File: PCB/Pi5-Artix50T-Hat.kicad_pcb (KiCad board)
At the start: 4 copper layers, 85 x 56 mm, 162 parts, among them J1 GPIO, J2 Molex 0878321420, J3 68711614522, J5 MIPI0, J6 MIPI1, U1 BL24C256A, U10 AP62200TWU-7, U11 AP62200TWU-7, U12 AP62200TWU-7, U2 XC7A50T-FGG484, U9 AP62200TWU-7, X1 50MHz

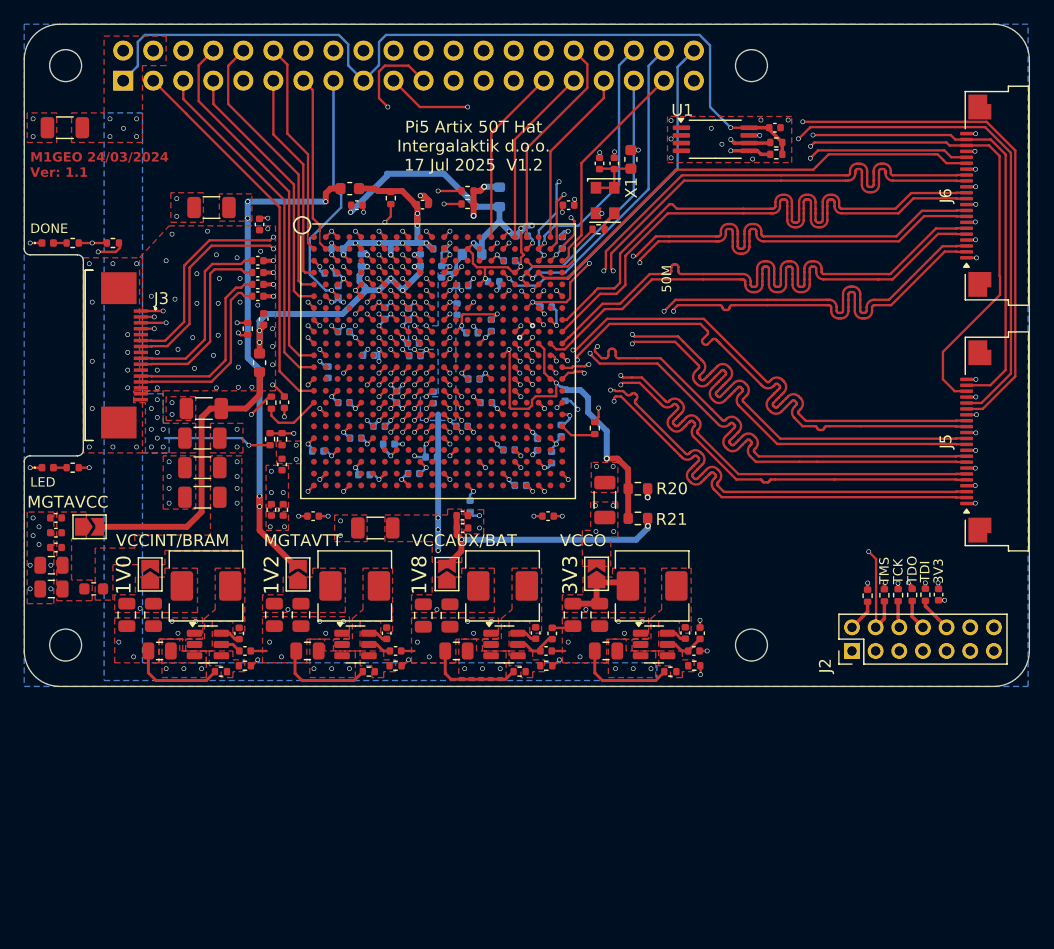
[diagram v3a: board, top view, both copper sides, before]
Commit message: MIPI conectors should be now compatible with C597981
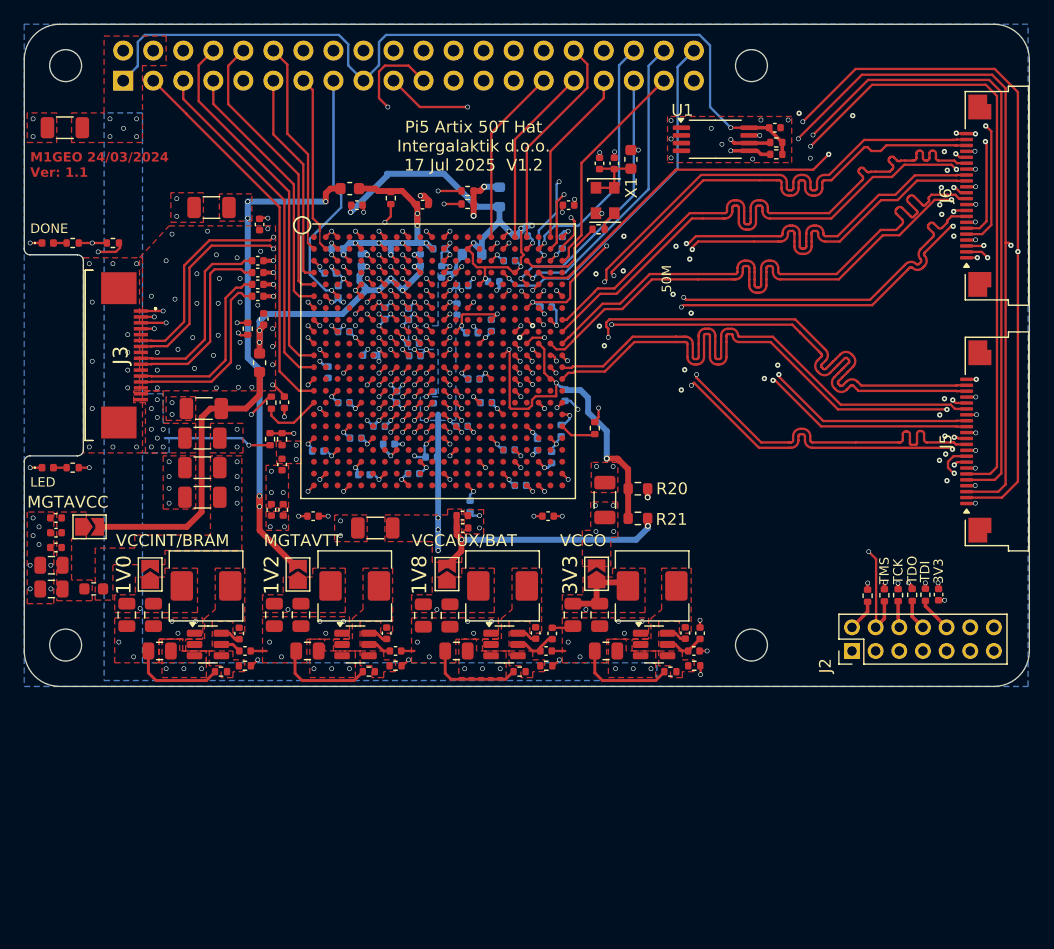
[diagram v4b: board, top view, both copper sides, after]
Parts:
- J3: footprint 68711614522:68711614522 -> Wurth_68711614522:68711614522
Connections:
- J5 pad 1: GND -> BANK_15_VCC
- J5 pad 11: /FPGA Top/FPGA Bank 15 & 16/MIPI0_D2+ -> /FPGA Top/FPGA Bank 15 & 16/MIPI0_D2-
- J5 pad 12: /FPGA Top/FPGA Bank 15 & 16/MIPI0_D2- -> /FPGA Top/FPGA Bank 15 & 16/MIPI0_D2+
- J5 pad 14: /FPGA Top/FPGA Bank 15 & 16/MIPI0_D1+ -> /FPGA Top/FPGA Bank 15 & 16/MIPI0_CK-
- J5 pad 15: /FPGA Top/FPGA Bank 15 & 16/MIPI0_D1- -> /FPGA Top/FPGA Bank 15 & 16/MIPI0_CK+
- J5 pad 17: /FPGA Top/FPGA Bank 15 & 16/MIPI0_CAM_GPIO0 -> /FPGA Top/FPGA Bank 15 & 16/MIPI0_D3-
- J5 pad 18: /FPGA Top/FPGA Bank 15 & 16/MIPI0_CAM_GPIO1 -> /FPGA Top/FPGA Bank 15 & 16/MIPI0_D3+
- J5 pad 2: /FPGA Top/FPGA Bank 15 & 16/MIPI0_D0+ -> /FPGA Top/FPGA Bank 15 & 16/SDA0
- J5 pad 20: /FPGA Top/FPGA Bank 15 & 16/SCL0 -> /FPGA Top/FPGA Bank 15 & 16/MIPI0_D0-
- J5 pad 21: /FPGA Top/FPGA Bank 15 & 16/SDA0 -> /FPGA Top/FPGA Bank 15 & 16/MIPI0_D0+
- J5 pad 22: BANK_15_VCC -> GND
- J5 pad 3: /FPGA Top/FPGA Bank 15 & 16/MIPI0_D0- -> /FPGA Top/FPGA Bank 15 & 16/SCL0
- J5 pad 5: /FPGA Top/FPGA Bank 15 & 16/MIPI0_D3+ -> /FPGA Top/FPGA Bank 15 & 16/MIPI0_CAM_GPIO1
- J5 pad 6: /FPGA Top/FPGA Bank 15 & 16/MIPI0_D3- -> /FPGA Top/FPGA Bank 15 & 16/MIPI0_CAM_GPIO0
- J5 pad 8: /FPGA Top/FPGA Bank 15 & 16/MIPI0_CK+ -> /FPGA Top/FPGA Bank 15 & 16/MIPI0_D1-
- J5 pad 9: /FPGA Top/FPGA Bank 15 & 16/MIPI0_CK- -> /FPGA Top/FPGA Bank 15 & 16/MIPI0_D1+
- J6 pad 1: GND -> BANK_15_VCC
- J6 pad 11: /FPGA Top/FPGA Bank 15 & 16/MIPI1_D2+ -> /FPGA Top/FPGA Bank 15 & 16/MIPI1_D2-
- J6 pad 12: /FPGA Top/FPGA Bank 15 & 16/MIPI1_D2- -> /FPGA Top/FPGA Bank 15 & 16/MIPI1_D2+
- J6 pad 14: /FPGA Top/FPGA Bank 15 & 16/MIPI1_D1+ -> /FPGA Top/FPGA Bank 15 & 16/MIPI1_CK-
- J6 pad 15: /FPGA Top/FPGA Bank 15 & 16/MIPI1_D1- -> /FPGA Top/FPGA Bank 15 & 16/MIPI1_CK+
- J6 pad 17: /FPGA Top/FPGA Bank 15 & 16/MIPI1_CAM_GPIO0 -> /FPGA Top/FPGA Bank 15 & 16/MIPI1_D3-
- J6 pad 18: /FPGA Top/FPGA Bank 15 & 16/MIPI1_CAM_GPIO1 -> /FPGA Top/FPGA Bank 15 & 16/MIPI1_D3+
- J6 pad 2: /FPGA Top/FPGA Bank 15 & 16/MIPI1_D0+ -> /FPGA Top/FPGA Bank 15 & 16/SDA0
- J6 pad 20: /FPGA Top/FPGA Bank 15 & 16/SCL0 -> /FPGA Top/FPGA Bank 15 & 16/MIPI1_D0-
- J6 pad 21: /FPGA Top/FPGA Bank 15 & 16/SDA0 -> /FPGA Top/FPGA Bank 15 & 16/MIPI1_D0+
- J6 pad 22: BANK_15_VCC -> GND
- J6 pad 3: /FPGA Top/FPGA Bank 15 & 16/MIPI1_D0- -> /FPGA Top/FPGA Bank 15 & 16/SCL0
- J6 pad 5: /FPGA Top/FPGA Bank 15 & 16/MIPI1_D3+ -> /FPGA Top/FPGA Bank 15 & 16/MIPI1_CAM_GPIO1
- J6 pad 6: /FPGA Top/FPGA Bank 15 & 16/MIPI1_D3- -> /FPGA Top/FPGA Bank 15 & 16/MIPI1_CAM_GPIO0
- J6 pad 8: /FPGA Top/FPGA Bank 15 & 16/MIPI1_CK+ -> /FPGA Top/FPGA Bank 15 & 16/MIPI1_D1-
- J6 pad 9: /FPGA Top/FPGA Bank 15 & 16/MIPI1_CK- -> /FPGA Top/FPGA Bank 15 & 16/MIPI1_D1+
- U2 pad B21: /FPGA Top/FPGA Bank 15 & 16/SCL0 -> /FPGA Top/FPGA Bank 15 & 16/MIPI0_CAM_GPIO0
- U2 pad C20: /FPGA Top/FPGA Bank 15 & 16/SDA0 -> /FPGA Top/FPGA Bank 15 & 16/MIPI0_CAM_GPIO1
- U2 pad F19: /FPGA Top/FPGA Bank 15 & 16/MIPI0_CAM_GPIO0 -> /FPGA Top/FPGA Bank 15 & 16/SDA0
- U2 pad F20: /FPGA Top/FPGA Bank 15 & 16/MIPI0_CAM_GPIO1 -> /FPGA Top/FPGA Bank 15 & 16/SCL0
- U2 pad G20: /FPGA Top/FPGA Bank 15 & 16/MIPI1_D1- -> /FPGA Top/FPGA Bank 15 & 16/MIPI1_D0-
- U2 pad H20: /FPGA Top/FPGA Bank 15 & 16/MIPI1_D1+ -> /FPGA Top/FPGA Bank 15 & 16/MIPI1_D0+
- U2 pad H22: /FPGA Top/FPGA Bank 15 & 16/MIPI1_D2- -> /FPGA Top/FPGA Bank 15 & 16/MIPI1_D3-
- U2 pad J22: /FPGA Top/FPGA Bank 15 & 16/MIPI1_D2+ -> /FPGA Top/FPGA Bank 15 & 16/MIPI1_D3+
- U2 pad K21: /FPGA Top/FPGA Bank 15 & 16/MIPI1_D3+ -> /FPGA Top/FPGA Bank 15 & 16/MIPI1_D2+
- U2 pad K22: /FPGA Top/FPGA Bank 15 & 16/MIPI1_D3- -> /FPGA Top/FPGA Bank 15 & 16/MIPI1_D2-
- U2 pad L18: /FPGA Top/FPGA Bank 15 & 16/MIPI0_D3- -> /FPGA Top/FPGA Bank 15 & 16/MIPI0_D2-
- U2 pad L19: /FPGA Top/FPGA Bank 15 & 16/MIPI0_D1+ -> /FPGA Top/FPGA Bank 15 & 16/MIPI0_D0+
- U2 pad L20: /FPGA Top/FPGA Bank 15 & 16/MIPI0_D1- -> /FPGA Top/FPGA Bank 15 & 16/MIPI0_D0-
- U2 pad L21: /FPGA Top/FPGA Bank 15 & 16/MIPI1_D0- -> /FPGA Top/FPGA Bank 15 & 16/MIPI1_D1-
- U2 pad M18: /FPGA Top/FPGA Bank 15 & 16/MIPI0_D3+ -> /FPGA Top/FPGA Bank 15 & 16/MIPI0_D2+
- U2 pad M21: /FPGA Top/FPGA Bank 15 & 16/MIPI1_D0+ -> /FPGA Top/FPGA Bank 15 & 16/MIPI1_D1+
- U2 pad M22: /FPGA Top/FPGA Bank 15 & 16/MIPI0_D2- -> /FPGA Top/FPGA Bank 15 & 16/MIPI0_D3-
- U2 pad N18: /FPGA Top/FPGA Bank 15 & 16/MIPI0_D0+ -> /FPGA Top/FPGA Bank 15 & 16/MIPI0_D1+
- U2 pad N19: /FPGA Top/FPGA Bank 15 & 16/MIPI0_D0- -> /FPGA Top/FPGA Bank 15 & 16/MIPI0_D1-
- U2 pad N22: /FPGA Top/FPGA Bank 15 & 16/MIPI0_D2+ -> /FPGA Top/FPGA Bank 15 & 16/MIPI0_D3+
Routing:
- net /FPGA Top/FPGA Bank 15 & 16/SDA0: track 69.9 -> 99.2 mm, vias 3 -> 4
- net /FPGA Top/FPGA Bank 15 & 16/SCL0: track 67.5 -> 95.6 mm, vias 2 -> 4
- net /FPGA Top/FPGA Bank 15 & 16/MIPI1_CAM_GPIO1: track 39.2 -> 52.5 mm, vias 2 -> 3
- net /FPGA Top/FPGA Bank 15 & 16/MIPI1_CAM_GPIO0: track 41.0 -> 51.5 mm, vias 0 -> 2
- net /FPGA Top/FPGA Bank 15 & 16/MIPI0_CAM_GPIO1: track 76.7 -> 84.6 mm, vias 2 -> 3
- net /FPGA Top/FPGA Bank 15 & 16/MIPI1_D3+: track 49.8 -> 46.9 mm, vias 0 -> 2
- net /FPGA Top/FPGA Bank 15 & 16/MIPI1_D2+: track 49.8 -> 47.1 mm, vias 0 -> 2
- net /FPGA Top/FPGA Bank 15 & 16/MIPI0_D2+: track 47.2 -> 44.5 mm, vias 2 -> 4
- net /FPGA Top/FPGA Bank 15 & 16/MIPI1_D1+: track 47.0 -> 44.3 mm, vias 2 -> 4
- net /FPGA Top/FPGA Bank 15 & 16/MIPI0_D1+: track 49.5 -> 47.1 mm
- net /FPGA Top/FPGA Bank 15 & 16/MIPI0_D0+: track 47.2 -> 48.5 mm
- net BANK_15_VCC: track 118.8 -> 120.0 mm
- net /FPGA Top/FPGA Bank 15 & 16/MIPI0_CAM_GPIO0: track 79.1 -> 80.1 mm
- net /FPGA Top/FPGA Bank 15 & 16/MIPI0_D3-: track 47.1 -> 46.4 mm, vias 2 -> 0
- net /FPGA Top/FPGA Bank 15 & 16/MIPI0_D2-: track 46.9 -> 47.5 mm
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
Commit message: Update
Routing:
- net /FPGA Top/FPGA Bank 15 & 16/MIPI0_CK-: track 47.0 -> 47.9 mm
- net /FPGA Top/FPGA Bank 15 & 16/MIPI0_CK+: track 47.1 -> 47.9 mm
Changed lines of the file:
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@@
 		(grid_origin 100 100)
 		(pcbplotparams
-			(layerselection 0x00000000_00000000_55555555_5755f5ff)
-			(plot_on_all_layers_selection 0x00000000_00000000_00000000_00000000)
+			(layerselection 0x00000000_00000000_55555555_575ff5ff)
+			(plot_on_all_layers_selection 0x00000000_00000000_00000000_02000000)
 			(disableapertmacros no)
 			(usegerberextensions yes)
@@
 			(drillshape 0)
 			(scaleselection 1)
-			(outputdirectory "outputs/")
+			(outputdirectory "production/gerbers/")
 		)
 	)
@@
 	)
 	(segment
+		(start 148.497812 68.590386)
+		(end 150.753198 66.335)
+		(width 0.2)
+		(layer "In2.Cu")
+		(net 313)
+	)
+	(segment
 		(start 145.869075 70.67)
 		(end 146.418198 70.67)
@@
 	)
 	(segment
-		(start 155.716801 66.335)
+		(start 157.87 68.488199)
 		(end 157.986946 68.605145)
 		(width 0.2)
@@
 	)
 	(segment
-		(start 148.497812 68.590386)
-		(end 150.753198 66.335)
-		(width 0.2)
-		(layer "In2.Cu")
-		(net 313)
-	)
-	(segment
 		(start 144.16 70.67)
 		(end 144.669075 70.67)
@@
 	)
 	(segment
+		(start 150.753198 66.335)
+		(end 157.125 66.335)
+		(width 0.2)
+		(layer "In2.Cu")
+		(net 313)
+	)
+	(segment
 		(start 163.322512 74.117488)
 		(end 163.322512 73.940711)
@@
 	)
 	(segment
-		(start 146.418198 70.67)
-		(end 146.877817 70.21038)
+		(start 157.125 66.335)
+		(end 157.87 67.08)
 		(width 0.2)
 		(layer "In2.Cu")
@@
 	)
 	(segment
-		(start 150.753198 66.335)
-		(end 155.716801 66.335)
+		(start 157.87 67.08)
+		(end 157.87 68.488199)
+		(width 0.2)
+		(layer "In2.Cu")
+		(net 313)
+	)
+	(segment
+		(start 146.418198 70.67)
+		(end 146.877817 70.21038)
 		(width 0.2)
 		(layer "In2.Cu")
@@
 	)
 	(segment
-		(start 158.305145 68.286946)
-		(end 155.903199 65.885)
+		(start 163.640711 73.622512)
+		(end 162.234014 72.215815)
 		(width 0.2)
 		(layer "In2.Cu")
@@
 	)
 	(segment
-		(start 163.640711 73.622512)
-		(end 162.234014 72.215815)
+		(start 146.381802 70.07)
+		(end 143.33 70.07)
+		(width 0.2)
+		(layer "In2.Cu")
+		(net 314)
+	)
+	(segment
+		(start 158.3 68.281801)
+		(end 158.3 66.91)
 		(width 0.2)
 		(layer "In2.Cu")
@@
 	)
 	(segment
-		(start 150.566802 65.885)
-		(end 146.381802 70.07)
+		(start 158.305145 68.286946)
+		(end 158.3 68.281801)
+		(width 0.2)
+		(layer "In2.Cu")
+		(net 314)
+	)
+	(segment
+		(start 158.3 66.91)
+		(end 157.275 65.885)
 		(width 0.2)
 		(layer "In2.Cu")
@@
 	)
 	(segment
+		(start 157.275 65.885)
+		(end 150.566802 65.885)
+		(width 0.2)
+		(layer "In2.Cu")
+		(net 314)
+	)
+	(segment
 		(start 163.817488 73.622512)
 		(end 163.640711 73.622512)
@@
 	)
 	(segment
-		(start 143.33 70.07)
-		(end 141.93 71.47)
+		(start 150.566802 65.885)
+		(end 146.381802 70.07)
 		(width 0.2)
 		(layer "In2.Cu")
@@
 	)
 	(segment
-		(start 155.903199 65.885)
-		(end 150.566802 65.885)
-		(width 0.2)
-		(layer "In2.Cu")
-		(net 314)
-	)
-	(segment
-		(start 146.381802 70.07)
-		(end 143.33 70.07)
+		(start 143.33 70.07)
+		(end 141.93 71.47)
 		(width 0.2)
 		(layer "In2.Cu")
@@
 		)
 		(initial_side "right")
-		(last_diff_pair_gap 0.250001)
+		(last_diff_pair_gap 0.25)
 		(last_netname "/FPGA Top/FPGA Bank 15 & 16/MIPI1_D2-")
 		(last_status "tuned")
@@
 		)
 		(initial_side "left")
-		(last_diff_pair_gap 0.250001)
+		(last_diff_pair_gap 0.25)
 		(last_netname "/FPGA Top/FPGA Bank 15 & 16/MIPI1_D1-")
 		(last_status "tuned")
@@
 		)
 		(initial_side "right")
-		(last_diff_pair_gap 0.250001)
+		(last_diff_pair_gap 0.25)
 		(last_netname "/FPGA Top/FPGA Bank 15 & 16/MIPI0_CK+")
 		(last_status "tuned")
